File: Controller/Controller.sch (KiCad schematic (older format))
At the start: 0 parts

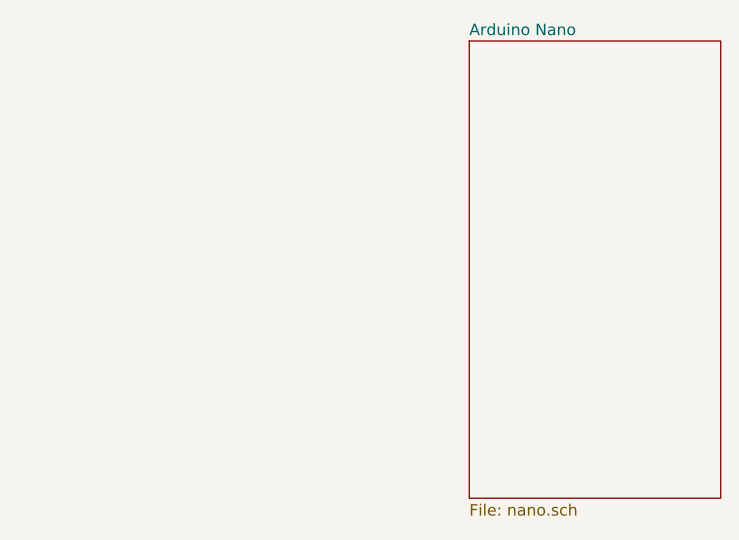
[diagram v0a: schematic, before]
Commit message: Add nano to main sheet
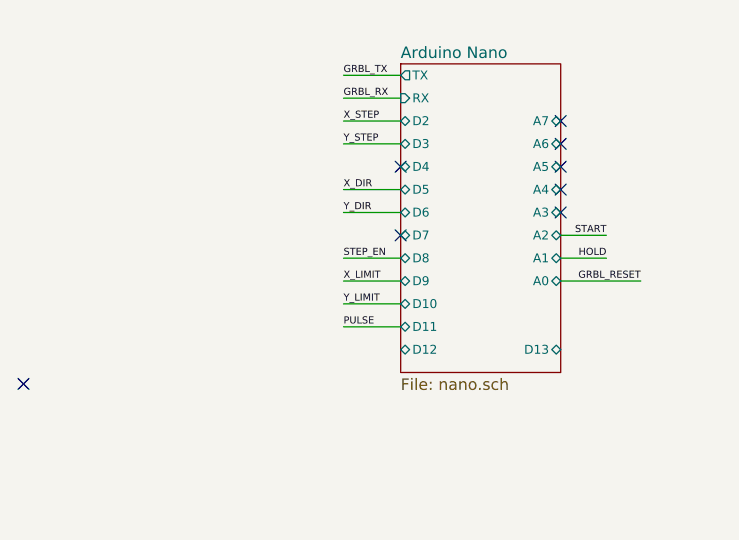
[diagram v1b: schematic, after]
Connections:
- no-connect marks 0 -> 8
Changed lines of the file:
@@
 EESchema Schematic File Version 4
+LIBS:Controller-cache
 EELAYER 29 0
 EELAYER END
@@
 $EndDescr
 $Sheet
-S 6900 2950 1100 2000
+S 6600 3050 700  1350
 U 5D499913
 F0 "Arduino Nano" 50
 F1 "nano.sch" 50
+F2 "D13" B R 7300 4300 39
+F3 "D12" B L 6600 4300 39
+F4 "D11" B L 6600 4200 39
+F5 "D10" B L 6600 4100 39
+F6 "D9" B L 6600 4000 39
+F7 "D8" B L 6600 3900 39
+F8 "D7" B L 6600 3800 39
+F9 "D6" B L 6600 3700 39
+F10 "D5" B L 6600 3600 39
+F11 "D4" B L 6600 3500 39
+F12 "D3" B L 6600 3400 39
+F13 "D2" B L 6600 3300 39
+F14 "A7" B R 7300 3300 39
+F15 "A6" B R 7300 3400 39
+F16 "A5" B R 7300 3500 39
+F17 "A4" B R 7300 3600 39
+F18 "A3" B R 7300 3700 39
+F19 "A2" B R 7300 3800 39
+F20 "A1" B R 7300 3900 39
+F21 "A0" B R 7300 4000 39
+F22 "TX" O L 6600 3100 39
+F23 "RX" I L 6600 3200 39
 $EndSheet
+Text Label 6350 3100 0    31   ~ 0
+GRBL_TX
+Text Label 6350 3200 0    31   ~ 0
+GRBL_RX
+Text Label 6350 3300 0    31   ~ 0
+X_STEP
+Text Label 6350 3400 0    31   ~ 0
+Y_STEP
+Text Label 6350 3600 0    31   ~ 0
+X_DIR
+Text Label 6350 3700 0    31   ~ 0
+Y_DIR
+Text Label 6350 3900 0    31   ~ 0
+STEP_EN
+Text Label 6350 4000 0    31   ~ 0
+X_LIMIT
+Text Label 6350 4100 0    31   ~ 0
+Y_LIMIT
+Text Label 6350 4200 0    31   ~ 0
+PULSE
+Text Label 7500 3800 2    31   ~ 0
+START
+Text Label 7500 3900 2    31   ~ 0
+HOLD
+Text Label 7650 4000 2    31   ~ 0
+GRBL_RESET
+Wire Wire Line
+	7300 4000 7650 4000
+Wire Wire Line
+	7500 3900 7300 3900
+Wire Wire Line
+	7300 3800 7500 3800
+Wire Wire Line
+	6350 3100 6600 3100
+Wire Wire Line
+	6600 3200 6350 3200
+Wire Wire Line
+	6350 3300 6600 3300
+Wire Wire Line
+	6600 3400 6350 3400
+Wire Wire Line
+	6350 3600 6600 3600
+Wire Wire Line
+	6600 3700 6350 3700
+Wire Wire Line
+	6350 3900 6600 3900
+Wire Wire Line
+	6600 4000 6350 4000
+Wire Wire Line
+	6350 4100 6600 4100
+Wire Wire Line
+	6600 4200 6350 4200
+NoConn ~ 6600 3500
+NoConn ~ 6600 3800
+NoConn ~ 7300 3300
+NoConn ~ 7300 3400
+NoConn ~ 7300 3500
+NoConn ~ 7300 3600
+NoConn ~ 7300 3700
+NoConn ~ 4950 4450
 $EndSCHEMATC
